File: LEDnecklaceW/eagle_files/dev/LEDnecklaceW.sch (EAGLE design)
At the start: 21 parts, among them P1 BU2032SM-BT-GCT

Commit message: LEDnecklaceW board and schematic updated to show component names for photocell and battery.
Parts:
- P1: value BU2032SM-BT-GCT -> (none)
- PC1: value PDV-P8101 -> (none)
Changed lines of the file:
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@@
 </classes>
 <parts>
-<part name="P1" library="freddyLibr" deviceset="BU2032SM-BT-GCT" device=""/>
 <part name="R1" library="resistor" deviceset="R-US_" device="R0603"/>
 <part name="R2" library="resistor" deviceset="R-US_" device="R0603"/>
-<part name="PC1" library="freddyLibr" deviceset="PDV-P8101" device=""/>
 <part name="D1" library="freddyLibr" deviceset="SZA05A0A" device=""/>
 <part name="R3" library="resistor" deviceset="R-US_" device="R0603"/>
@@
 <part name="R9" library="resistor" deviceset="R-US_" device="R0603"/>
 <part name="R10" library="resistor" deviceset="R-US_" device="R0603"/>
+<part name="P1" library="freddyLibr" deviceset="BU2032SM-BT-GCT" device=""/>
+<part name="PC1" library="freddyLibr" deviceset="PDV-P8101" device=""/>
 </parts>
 <sheets>
@@
 </plain>
 <instances>
-<instance part="P1" gate="G$1" x="-7.62" y="73.66"/>
 <instance part="R1" gate="G$1" x="15.24" y="76.2" rot="R90"/>
 <instance part="R2" gate="G$1" x="43.18" y="35.56" rot="R90"/>
-<instance part="PC1" gate="G$1" x="15.24" y="53.34"/>
 <instance part="D1" gate="G$1" x="43.18" y="53.34"/>
 <instance part="R3" gate="G$1" x="60.96" y="35.56" rot="R90"/>
@@
 <instance part="R9" gate="G$1" x="157.48" y="35.56" rot="R90"/>
 <instance part="R10" gate="G$1" x="172.72" y="35.56" rot="R90"/>
+<instance part="P1" gate="G$1" x="-7.62" y="73.66"/>
+<instance part="PC1" gate="G$1" x="15.24" y="53.34"/>
 </instances>
 <busses>
@@
 <net name="N$1" class="0">
 <segment>
-<pinref part="P1" gate="G$1" pin="VCC"/>
 <wire x1="-7.62" y1="81.28" x2="-7.62" y2="86.36" width="0.1524" layer="91"/>
 <pinref part="R1" gate="G$1" pin="2"/>
 <wire x1="-7.62" y1="86.36" x2="15.24" y2="86.36" width="0.1524" layer="91"/>
 <wire x1="15.24" y1="86.36" x2="15.24" y2="81.28" width="0.1524" layer="91"/>
+<pinref part="P1" gate="G$1" pin="VCC"/>
 </segment>
 </net>
 <net name="N$2" class="0">
 <segment>
-<pinref part="P1" gate="G$1" pin="GND"/>
 <wire x1="-7.62" y1="66.04" x2="-7.62" y2="25.4" width="0.1524" layer="91"/>
 <wire x1="-7.62" y1="25.4" x2="15.24" y2="25.4" width="0.1524" layer="91"/>
-<pinref part="PC1" gate="G$1" pin="2"/>
 <wire x1="15.24" y1="45.72" x2="15.24" y2="25.4" width="0.1524" layer="91"/>
 <pinref part="R10" gate="G$1" pin="1"/>
@@
 <pinref part="R2" gate="G$1" pin="1"/>
 <wire x1="43.18" y1="30.48" x2="43.18" y2="25.4" width="0.1524" layer="91"/>
+<pinref part="P1" gate="G$1" pin="GND"/>
+<pinref part="PC1" gate="G$1" pin="2"/>
 </segment>
 </net>
@@
 <net name="N$15" class="0">
 <segment>
-<pinref part="PC1" gate="G$1" pin="1"/>
 <pinref part="R1" gate="G$1" pin="1"/>
 <wire x1="15.24" y1="71.12" x2="15.24" y2="66.04" width="0.1524" layer="91"/>
@@
 <pinref part="D1" gate="G$1" pin="AD"/>
 <wire x1="43.18" y1="60.96" x2="43.18" y2="66.04" width="0.1524" layer="91"/>
+<pinref part="PC1" gate="G$1" pin="1"/>
 </segment>
 </net>

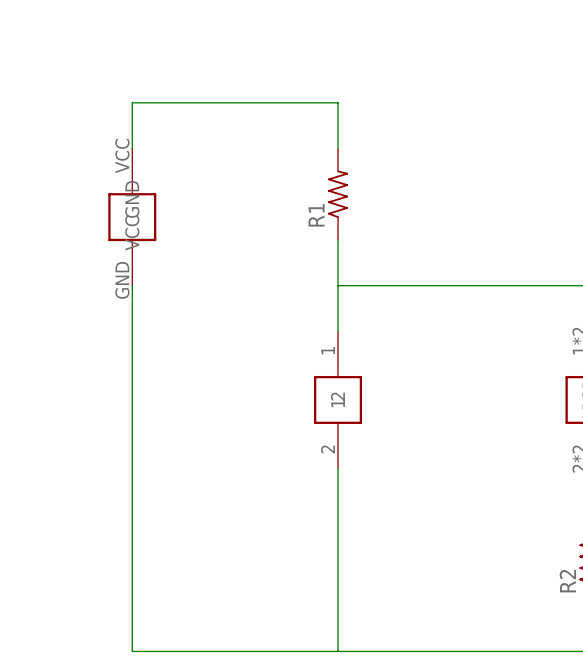
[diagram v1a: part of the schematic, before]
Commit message: Added switch to board and schematic. Also added output production files corresponding to these changes.
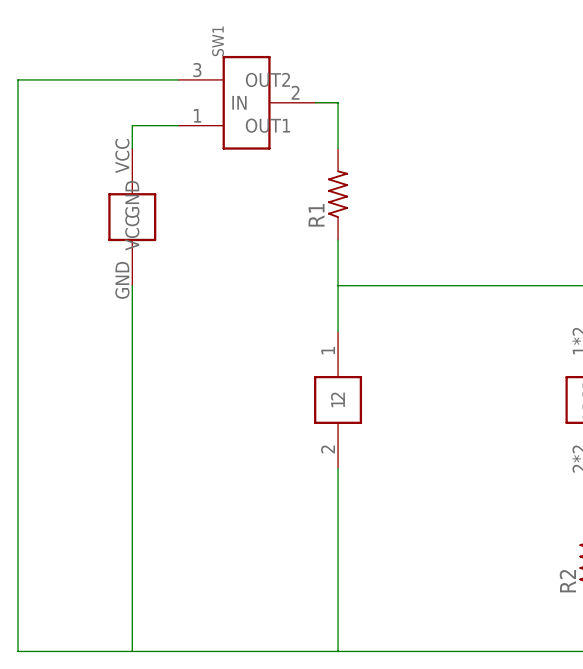
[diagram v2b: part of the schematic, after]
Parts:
- added SW1: PCM12SMTR, freddyLibr:PCM12SMTR
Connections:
- new net N$6: P1.VCC, SW1.OUT1
- net N$1: now also SW1.IN; no longer P1.VCC
- net N$2: now also SW1.OUT2
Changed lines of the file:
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@@
 <part name="P1" library="freddyLibr" deviceset="BU2032SM-BT-GCT" device=""/>
 <part name="PC1" library="freddyLibr" deviceset="PDV-P8101" device=""/>
+<part name="SW1" library="freddyLibr" deviceset="PCM12SMTR" device=""/>
 </parts>
 <sheets>
@@
 <instance part="P1" gate="G$1" x="-7.62" y="73.66"/>
 <instance part="PC1" gate="G$1" x="15.24" y="53.34"/>
+<instance part="SW1" gate="G$1" x="5.08" y="86.36" rot="R90"/>
 </instances>
 <busses>
 </busses>
 <nets>
-<net name="N$1" class="0">
-<segment>
-<wire x1="-7.62" y1="81.28" x2="-7.62" y2="86.36" width="0.1524" layer="91"/>
-<pinref part="R1" gate="G$1" pin="2"/>
-<wire x1="-7.62" y1="86.36" x2="15.24" y2="86.36" width="0.1524" layer="91"/>
-<wire x1="15.24" y1="86.36" x2="15.24" y2="81.28" width="0.1524" layer="91"/>
-<pinref part="P1" gate="G$1" pin="VCC"/>
-</segment>
-</net>
 <net name="N$2" class="0">
 <segment>
@@
 <pinref part="P1" gate="G$1" pin="GND"/>
 <pinref part="PC1" gate="G$1" pin="2"/>
+<pinref part="SW1" gate="G$1" pin="OUT2"/>
+<wire x1="-2.54" y1="88.9" x2="-20.32" y2="88.9" width="0.1524" layer="91"/>
+<wire x1="-20.32" y1="88.9" x2="-20.32" y2="25.4" width="0.1524" layer="91"/>
+<wire x1="-20.32" y1="25.4" x2="-7.62" y2="25.4" width="0.1524" layer="91"/>
 </segment>
 </net>
@@
 </segment>
 </net>
+<net name="N$1" class="0">
+<segment>
+<pinref part="R1" gate="G$1" pin="2"/>
+<wire x1="15.24" y1="81.28" x2="15.24" y2="86.36" width="0.1524" layer="91"/>
+<pinref part="SW1" gate="G$1" pin="IN"/>
+<wire x1="15.24" y1="86.36" x2="12.7" y2="86.36" width="0.1524" layer="91"/>
+</segment>
+</net>
+<net name="N$6" class="0">
+<segment>
+<pinref part="P1" gate="G$1" pin="VCC"/>
+<wire x1="-7.62" y1="81.28" x2="-7.62" y2="83.82" width="0.1524" layer="91"/>
+<pinref part="SW1" gate="G$1" pin="OUT1"/>
+<wire x1="-7.62" y1="83.82" x2="-2.54" y2="83.82" width="0.1524" layer="91"/>
+</segment>
+</net>
